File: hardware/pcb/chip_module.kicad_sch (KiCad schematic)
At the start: 17 parts, among them J1 Samtec LSHM-130, U1 ADG732BCPZ, U2 ADG732BCPZ, U3 ADA4530-1, U4 74LVC1G04, U5 QSSC_Chip

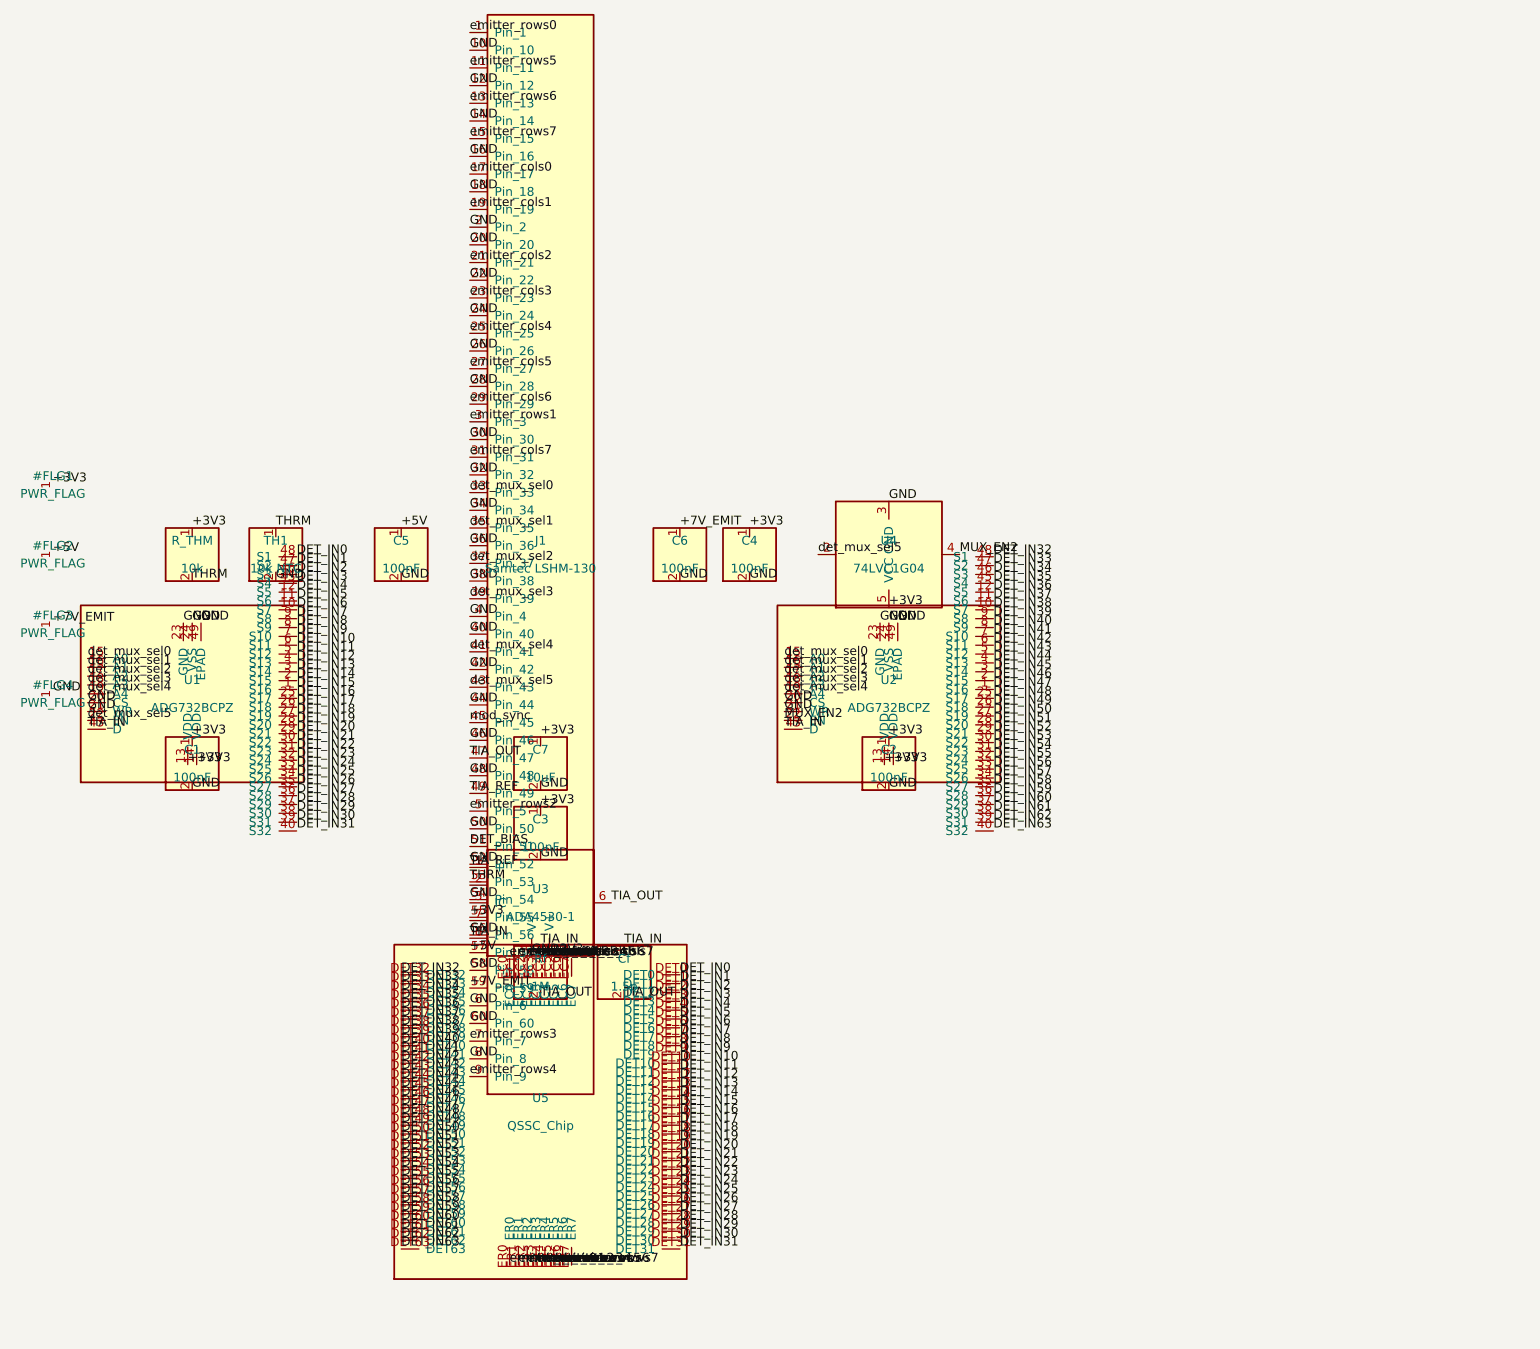
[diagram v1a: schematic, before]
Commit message: chip module: place discrete MOSFET emitter crossbar (+5V), eliminate +7V_EMIT
Emitter driver for the 8x8 CQD matrix is now placed on the swappable chip
module as the simplest-functional topology (29 parts, no boost / no DAC /
no TLC5955): 2x 74HCT240 inverting level-shifters (3.3V FPGA -> 0/5V gate
drive, HCT TTL thresholds) + 8x AO3401A P-MOS high-side row switches +
8x AO3400A N-MOS low-side column sinks + 8x 220R set resistors + 3
decoupling. One pixel at a time, ~9mA at 2.2V headroom, matching
emitter_array.v (rows active-HIGH / cols active-LOW one-hot, idle all OFF).

Chip ER/EC pads rewired through the driver (ER{i}->emitter_anode{i},
EC{i}->emitter_cathode{i}); J1 still carries emitter_rows/cols -> 74HCT240
inputs. +7V_EMIT rail fully deleted on both boards: J1/J11 pin 59 -> GND
(extra pulsed-current return; connectors stay pin-for-pin mated), module
POWER_PINS/POWER_NETS/C6/#FLG3 removed. TIA is photovoltaic / zero-bias
(no MCP4921 DAC; DET_BIAS is a reserved spare). Module widened 70->85x50mm.

Verified headless: module ERC 0 errors / 53 warnings; module DRC 0
violations; main board ERC 0 errors / 139 warnings, DRC 0 violations.
pytest 122 passed / 2 skipped; ruff CI-gate clean. HARDWARE_DESIGN.md
\S1B/\S2/\S3/\S7/\S8/\S11/\S12/\S13/\S15A updated. RTL/XDC/sim/synth
untouched; new ~24 nets not yet routed (deferred GUI batch).

Co-Authored-By: Claude <noreply@anthropic.com>
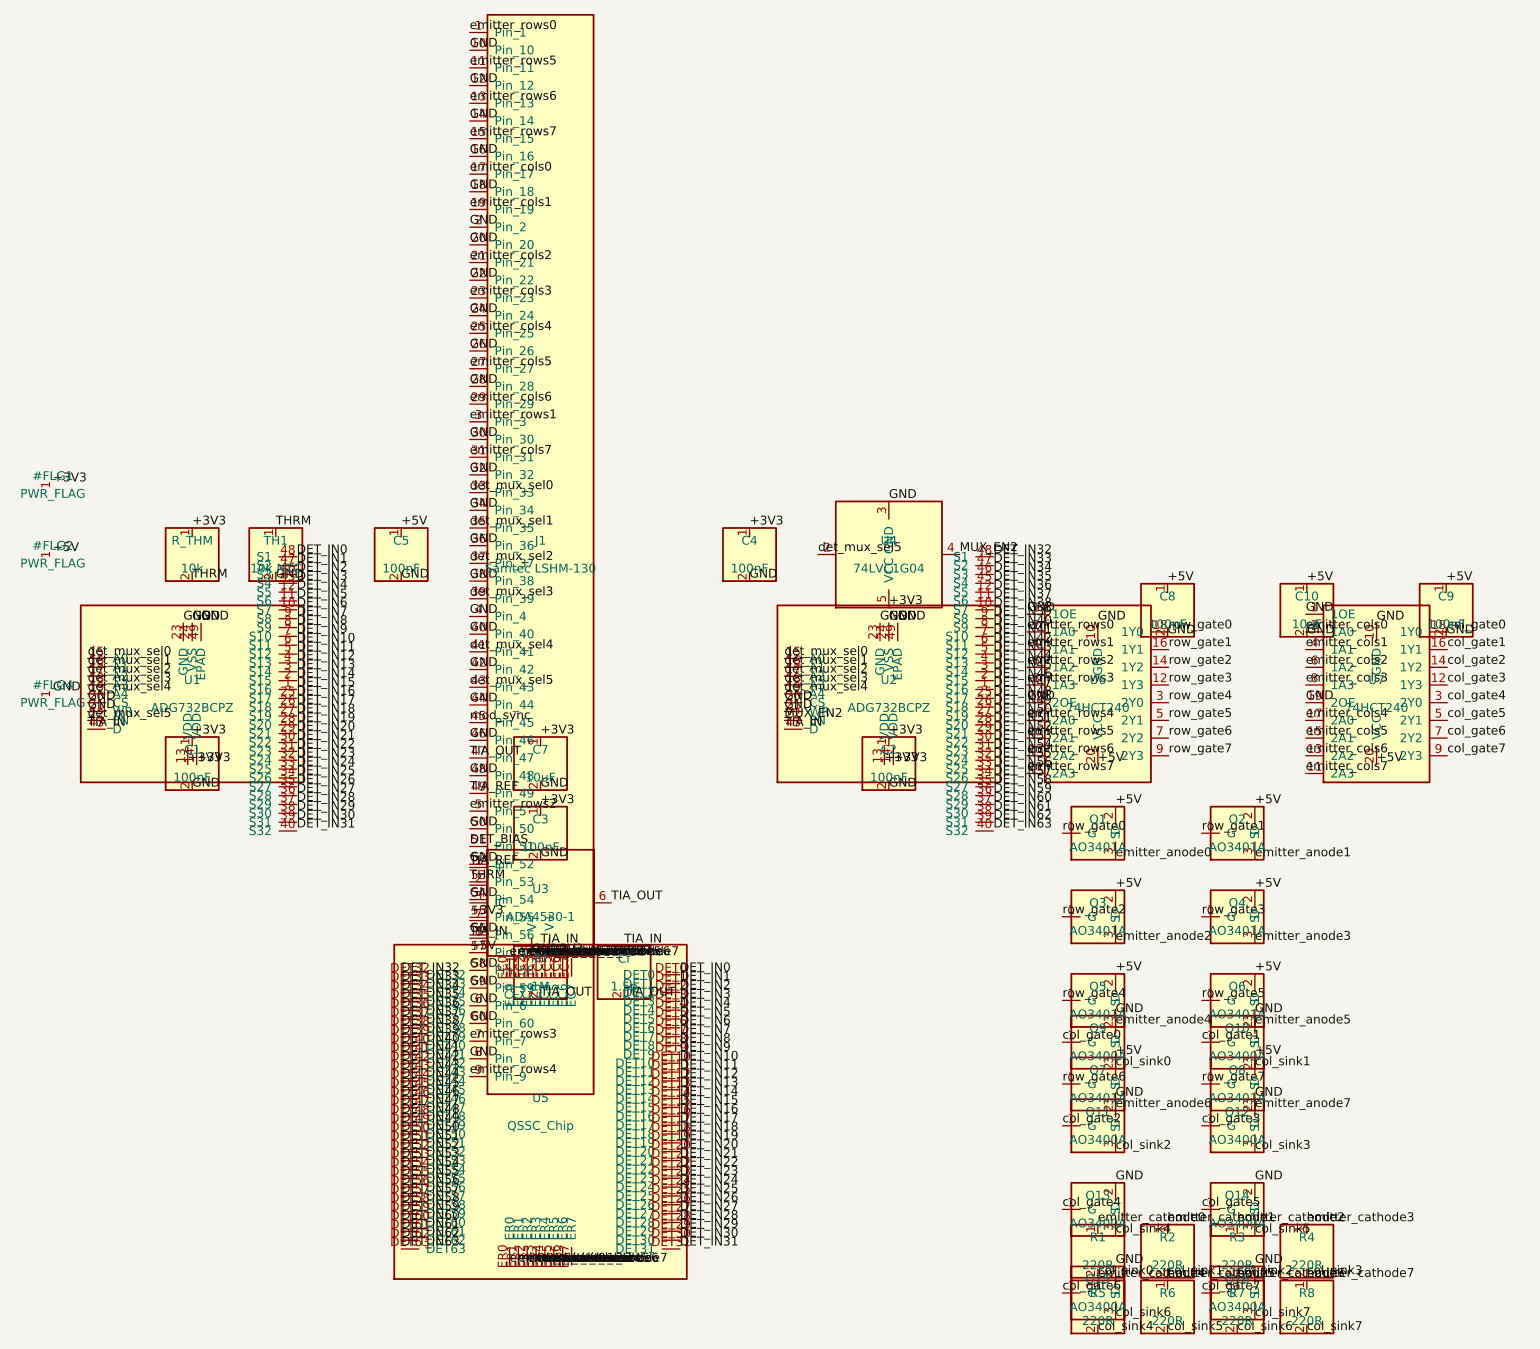
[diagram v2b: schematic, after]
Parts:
- removed C6: 100nF, Capacitor_SMD:C_0603_1608Metric, symbol qssc:C
- added C10: 10uF, Capacitor_SMD:C_0805_2012Metric, symbol qssc:C
- added C8, C9: 100nF, Capacitor_SMD:C_0603_1608Metric, symbol qssc:C
- added Q1, Q2, Q3, Q4, Q5, Q6, Q7, Q8: AO3401A, Package_TO_SOT_SMD:SOT-23_Handsoldering, symbol qssc:AO3401A
- added Q10, Q11, Q12, Q13, Q14, Q15, Q16, Q9: AO3400A, Package_TO_SOT_SMD:SOT-23_Handsoldering, symbol qssc:AO3400A
- added R1, R2, R3, R4, R5, R6, R7, R8: 220R, Resistor_SMD:R_0603_1608Metric, symbol qssc:R
- added U6, U7: 74HCT240, Package_SO:TSSOP-20_4.4x6.5mm_P0.65mm, symbol qssc:74HCT240
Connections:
- net +7V_EMIT is gone; now on net GND: J1.59 (Pin_59)
- net +5V: now also C10.1, C8.1, C9.1, Q1.2 (S), Q2.2 (S), Q3.2 (S), Q4.2 (S), Q5.2 (S), Q6.2 (S), Q7.2 (S), Q8.2 (S), U6.20 (VCC), U7.20 (VCC)
- net GND: now also C10.2, C8.2, C9.2, Q10.2 (S), Q11.2 (S), Q12.2 (S), Q13.2 (S), Q14.2 (S), Q15.2 (S), Q16.2 (S), Q9.2 (S), U6.1 (1OE), U6.10 (GND), U6.19 (2OE), U7.1 (1OE), U7.10 (GND), U7.19 (2OE)
- net emitter_cols0: now also U7.2 (1A0); no longer U5.EC0
- net emitter_cols1: now also U7.4 (1A1); no longer U5.EC1
- net emitter_cols2: now also U7.6 (1A2); no longer U5.EC2
- net emitter_cols3: now also U7.8 (1A3); no longer U5.EC3
- net emitter_cols4: now also U7.17 (2A0); no longer U5.EC4
- net emitter_cols5: now also U7.15 (2A1); no longer U5.EC5
- net emitter_cols6: now also U7.13 (2A2); no longer U5.EC6
- net emitter_cols7: now also U7.11 (2A3); no longer U5.EC7
- net emitter_rows0: now also U6.2 (1A0); no longer U5.ER0
- net emitter_rows1: now also U6.4 (1A1); no longer U5.ER1
- net emitter_rows2: now also U6.6 (1A2); no longer U5.ER2
- net emitter_rows3: now also U6.8 (1A3); no longer U5.ER3
- net emitter_rows4: now also U6.17 (2A0); no longer U5.ER4
- net emitter_rows5: now also U6.15 (2A1); no longer U5.ER5
- net emitter_rows6: now also U6.13 (2A2); no longer U5.ER6
- net emitter_rows7: now also U6.11 (2A3); no longer U5.ER7
- new net col_gate0: Q9.1 (G), U7.18 (1Y0)
- new net col_gate1: Q10.1 (G), U7.16 (1Y1)
- new net col_gate2: Q11.1 (G), U7.14 (1Y2)
- new net col_gate3: Q12.1 (G), U7.12 (1Y3)
- new net col_gate4: Q13.1 (G), U7.3 (2Y0)
- new net col_gate5: Q14.1 (G), U7.5 (2Y1)
- new net col_gate6: Q15.1 (G), U7.7 (2Y2)
- new net col_gate7: Q16.1 (G), U7.9 (2Y3)
- new net col_sink0: Q9.3 (D), R1.2
- new net col_sink1: Q10.3 (D), R2.2
- new net col_sink2: Q11.3 (D), R3.2
- new net col_sink3: Q12.3 (D), R4.2
- new net col_sink4: Q13.3 (D), R5.2
- new net col_sink5: Q14.3 (D), R6.2
- new net col_sink6: Q15.3 (D), R7.2
- new net col_sink7: Q16.3 (D), R8.2
- new net emitter_anode0: Q1.3 (D), U5.ER0
- new net emitter_anode1: Q2.3 (D), U5.ER1
- new net emitter_anode2: Q3.3 (D), U5.ER2
- new net emitter_anode3: Q4.3 (D), U5.ER3
- new net emitter_anode4: Q5.3 (D), U5.ER4
- new net emitter_anode5: Q6.3 (D), U5.ER5
- new net emitter_anode6: Q7.3 (D), U5.ER6
- new net emitter_anode7: Q8.3 (D), U5.ER7
- new net emitter_cathode0: R1.1, U5.EC0
- new net emitter_cathode1: R2.1, U5.EC1
- new net emitter_cathode2: R3.1, U5.EC2
- new net emitter_cathode3: R4.1, U5.EC3
- new net emitter_cathode4: R5.1, U5.EC4
- new net emitter_cathode5: R6.1, U5.EC5
- new net emitter_cathode6: R7.1, U5.EC6
- new net emitter_cathode7: R8.1, U5.EC7
- new net row_gate0: Q1.1 (G), U6.18 (1Y0)
- new net row_gate1: Q2.1 (G), U6.16 (1Y1)
- new net row_gate2: Q3.1 (G), U6.14 (1Y2)
- new net row_gate3: Q4.1 (G), U6.12 (1Y3)
- new net row_gate4: Q5.1 (G), U6.3 (2Y0)
- new net row_gate5: Q6.1 (G), U6.5 (2Y1)
- new net row_gate6: Q7.1 (G), U6.7 (2Y2)
- new net row_gate7: Q8.1 (G), U6.9 (2Y3)
